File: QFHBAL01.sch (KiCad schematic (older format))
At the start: 10 parts, among them J1 Conn_Coaxial, T1 Transformer_1P_SS

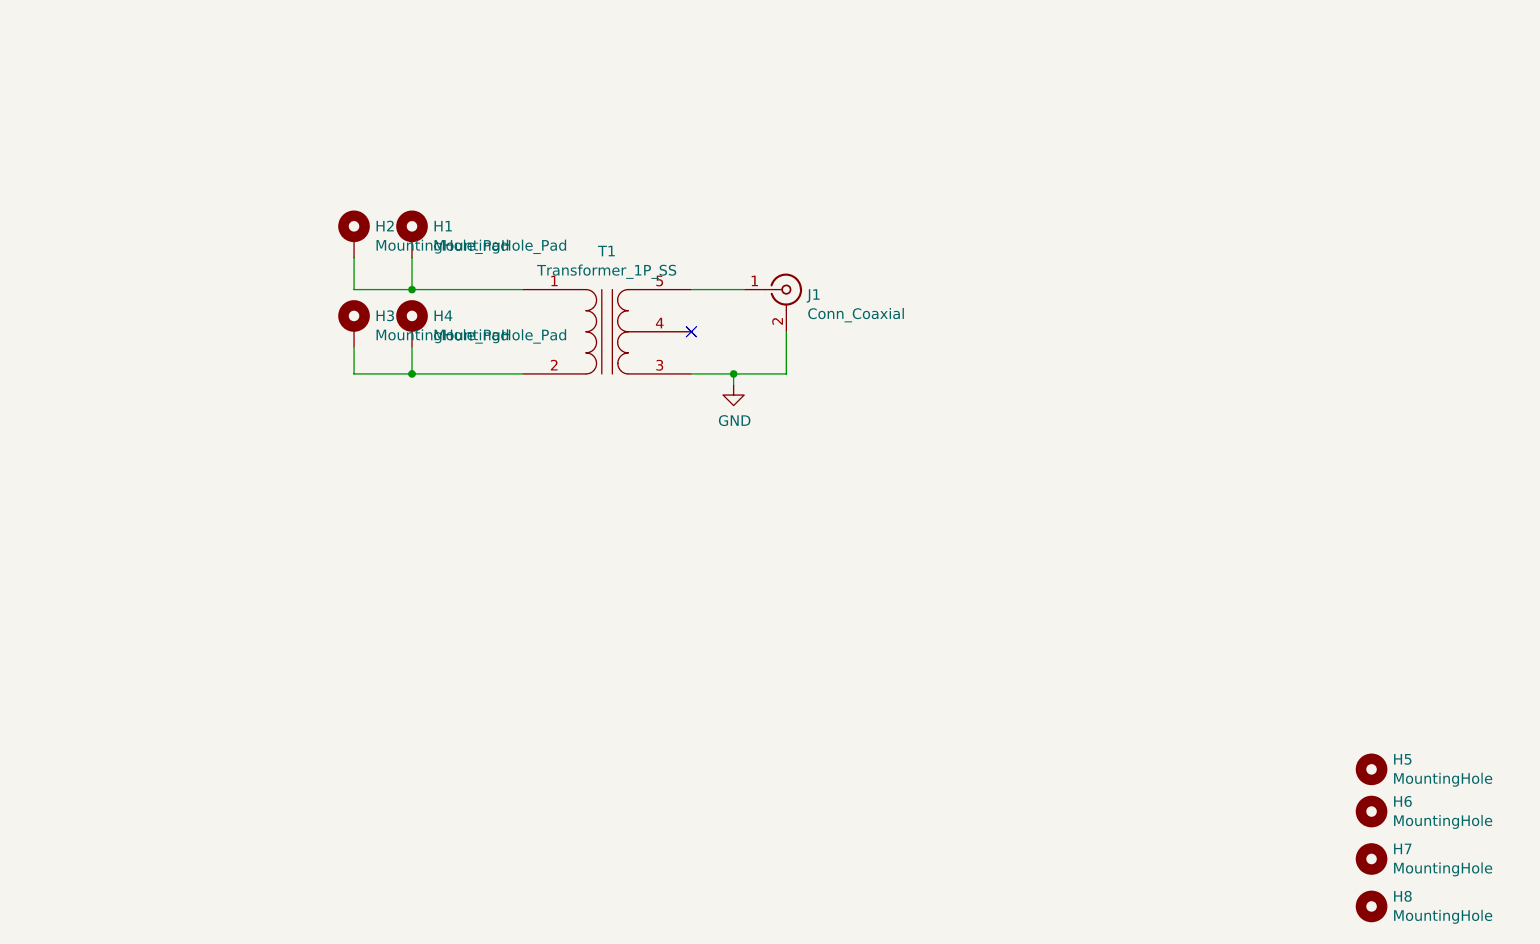
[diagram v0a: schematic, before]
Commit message: Solved issue #1: Layout upraven pro moznost zapojeni jako "common mode" a "trafo".
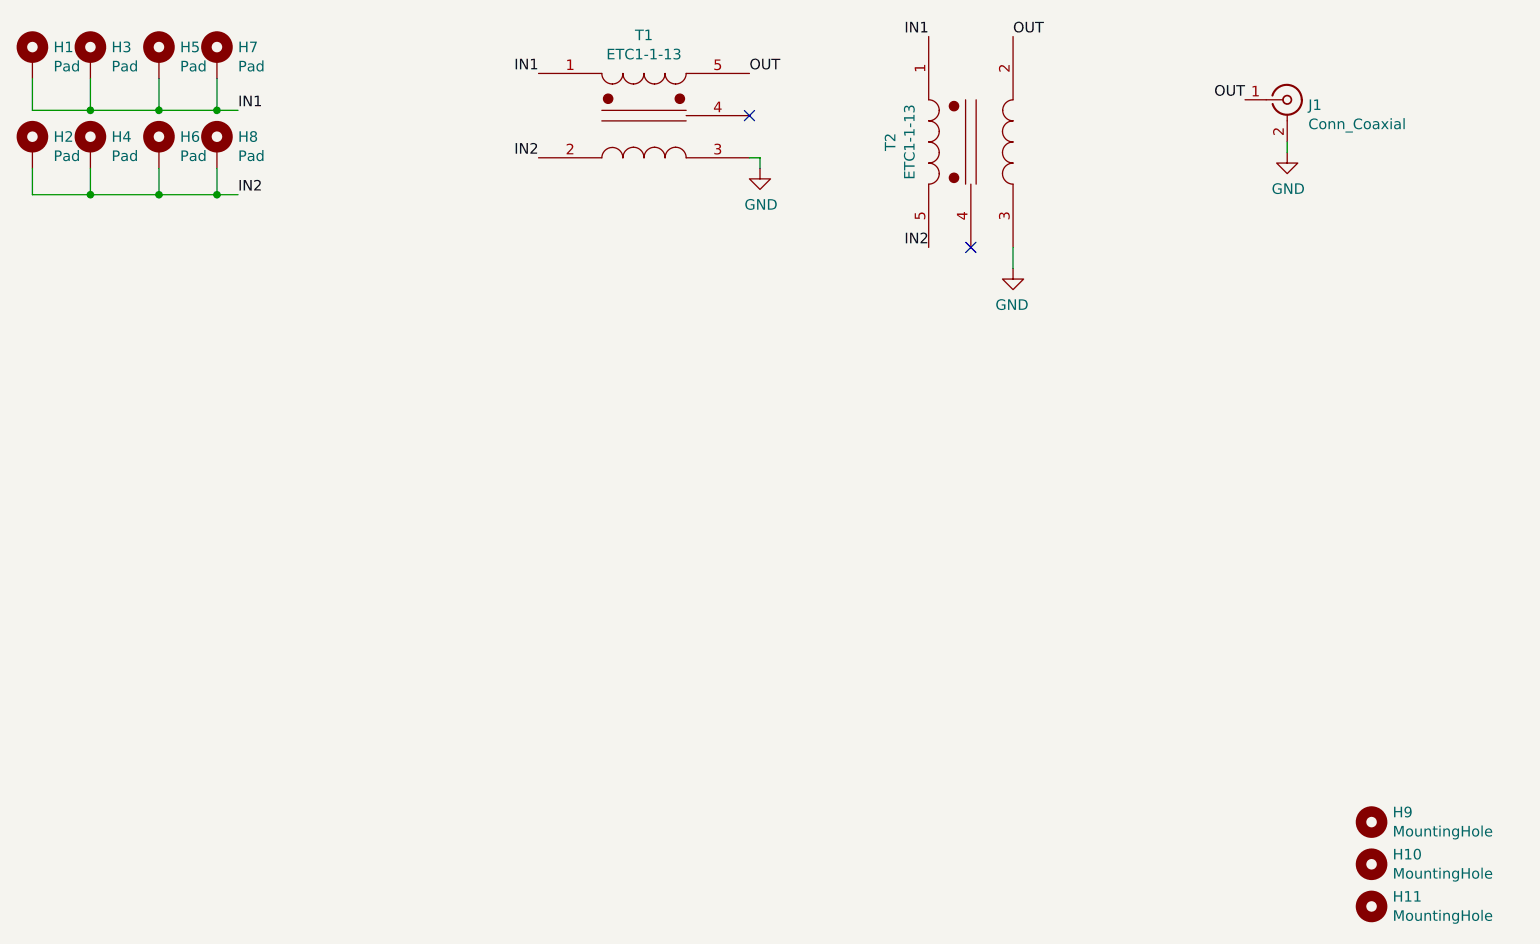
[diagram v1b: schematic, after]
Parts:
- removed H7: MountingHole, MountingHole:MountingHole_3.2mm_M3, symbol Mechanical:MountingHole
- removed T1: Transformer_1P_SS, Transformer_SMD:Transformer_MACOM_SM-22, symbol Device:Transformer_1P_SS
- added H2, H4, H6, H8: Pad, MountingHole:MountingHole_2.2mm_M2_Pad, symbol Mechanical:MountingHole_Pad
- added T1, T2: ETC1-1-13, Transformer_SMD:Transformer_MACOM_SM-22, symbol riske-symbols:ETC1-1-13
- H1: renamed from H2; value MountingHole_Pad -> Pad
- H3: renamed from H1; value MountingHole_Pad -> Pad
- H5: renamed from H3; value MountingHole_Pad -> Pad
- H7: renamed from H4; value MountingHole_Pad -> Pad
- renumbered H6 to H10, H8 to H11, H5 to H9
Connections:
- net GND: now also T1.3 (SA), T2.3 (SA)
- net IN1: now reaches H1.1, H3.1
- net IN1: now also H5.1, H7.1, T1.1 (AA), T2.1 (AA)
- net OUT: now reaches J1.1 (In)
- net OUT: now also T1.5 (SB), T2.2 (AB)
- new net IN2: H2.1, H4.1, H6.1, H8.1, T1.2 (AB), T2.5 (SB)
- no-connect marks 1 -> 2
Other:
- moved on the sheet: H1, H10, H3, H5, H7, H9, J1
